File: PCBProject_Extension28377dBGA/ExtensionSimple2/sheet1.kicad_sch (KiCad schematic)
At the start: 86 parts, among them P1 Header 6X2, P2 Header 6X2, P3 Header 2X2, P4 Header 2X2, P5 Header 2X2, P6 Header 2X2, Q1 FMMT618TA, U1 SN74ABT541, U2 SN74ABT541

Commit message: block routing done.
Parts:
- removed P3, P4, P5, P6: Header 2X2, Connector_PinSocket_2.54mm:PinSocket_2x02_P2.54mm_Vertical, symbol sheet1-altium-import:root_0_Header 2X2
- added J1: Conn_02x08_Top_Bottom, Connector_PinSocket_2.54mm:PinSocket_2x08_P2.54mm_Vertical, symbol Connector_Generic:Conn_02x08_Odd_Even
- added J2 (x2): Conn_01x02_Pin, Connector_PinSocket_2.54mm:PinSocket_2x02_P2.54mm_Vertical, symbol Connector_Generic:Conn_02x02_Odd_Even
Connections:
- net AGND: now also J1.1 (Pin_1), J1.11 (Pin_11), J1.3 (Pin_3), J1.5 (Pin_5), J1.7 (Pin_7), J1.9 (Pin_9)
- net D12V1: now also J1.14 (Pin_14), J1.16 (Pin_16)
- net DC_BUS_2M1: now also J2.1 (Pin_1), J2.3 (Pin_3)
- net DC_BUS_2M2: now also J2.1 (Pin_1), J2.3 (Pin_3)
- net GND_2M1: now also J2.2 (Pin_2), J2.4 (Pin_4)
- net GND_2M2: now also J2.2 (Pin_2), J2.4 (Pin_4)
- net PWM1A_5V: now also J1.2 (Pin_2)
- net PWM1B_5V: now also J1.8 (Pin_8)
- net PWM2A_5V: now also J1.4 (Pin_4)
- net PWM2B_5V: now also J1.10 (Pin_10)
- net PWM3A_5V: now also J1.6 (Pin_6)
- net PWM3B_5V: now also J1.12 (Pin_12)
- new net D12VGND: J1.13 (Pin_13), J1.15 (Pin_15)
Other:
- note added: "PWM信号&供电"

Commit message: update sheet1
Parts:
- removed P1, P2: Header 6X2, Connector_PinSocket_2.54mm:PinSocket_2x06_P2.54mm_Vertical, symbol sheet1-altium-import:root_0_Header 6X2
- added INC2, SPI1: HIF3FC-20PA-2.54DSA, Connector_IDC:IDC-Header_2x10_P2.54mm_Vertical, symbol sheet1-altium-import:root_0_HIF3FC-20PA-2.54DSA
- added J1: Conn_02x08_Top_Bottom, Connector_PinSocket_2.54mm:PinSocket_2x08_P2.54mm_Vertical, symbol Connector_Generic:Conn_02x08_Odd_Even
- added RU3: 0R, mmlab-footprint-library:0805, symbol sheet1-altium-import:root_0_Res2
- added SPI2: Conn_02x04_Counter_Clockwise, Connector_PinSocket_2.54mm:PinSocket_2x04_P2.54mm_Vertical, symbol Connector_Generic:Conn_02x04_Counter_Clockwise
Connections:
- net A+5V: now also SPI1.18, SPI1.20
- net AGND: now also J1.1 (Pin_1), J1.11 (Pin_11), J1.3 (Pin_3), J1.5 (Pin_5), J1.7 (Pin_7), J1.9 (Pin_9), SPI1.5, SPI1.7, SPI2.5 (Pin_5), SPI2.6 (Pin_6)
- net D+5V: now also SPI1.14, SPI1.16, SPI2.3 (Pin_3), SPI2.4 (Pin_4)
- net D12V1: now also J1.14 (Pin_14), J1.16 (Pin_16)
- net D12VGND: now also J1.13 (Pin_13), J1.15 (Pin_15)
- net PE_GND: now also SPI1.6, SPI1.8
- net PWM4A_5V: now also J1.2 (Pin_2)
- net PWM4B_5V: now also J1.8 (Pin_8)
- net PWM5A_5V: now also J1.4 (Pin_4)
- net PWM5B_5V: now also J1.10 (Pin_10)
- net PWM6A_5V: now also J1.6 (Pin_6)
- net PWM6B_5V: now also J1.12 (Pin_12)
- net REF_3V: now also RU3.1
- net SPI B MI HS: now also SPI2.2 (Pin_2)
- net SPI B MO HS: now also SPI2.1 (Pin_1)
- net SPI_A_CK_HS: now also SPI1.11
- net SPI_A_MI_HS: now also SPI1.12
- net SPI_A_MO_HS: now also SPI1.9
- net SPI_B_CK_HS: now also SPI2.8 (Pin_8)
- net SPI_C_CK_HS: now also SPI1.3
- net SPI_C_MI_HS: now also SPI1.4
- net SPI_C_MO_HS: now also SPI1.1
- net ~{SPI_A_STE_HS}: now also SPI1.10
- net ~{SPI_B_STE_HS}: now also SPI2.7 (Pin_7)
- net ~{SPI_C_STE_HS}: now also SPI1.2
- new net: RU3.2, SPI1.13, SPI1.15
- new net -5V_ADC: SPI1.17, SPI1.19
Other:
- note added: "DAC"

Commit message: extension board layout
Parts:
- removed INC2: HIF3FC-20PA-2.54DSA, Connector_IDC:IDC-Header_2x10_P2.54mm_Vertical, symbol sheet1-altium-import:root_0_HIF3FC-20PA-2.54DSA
- added J1: Conn_02x05_Odd_Even, Connector_IDC:IDC-Header_2x05_P2.54mm_Vertical, symbol Connector_Generic:Conn_02x05_Odd_Even
- LEM1, LEM2: footprint Connector_IDC:IDC-Header_2x15_P2.54mm_Vertical -> Connector_PinSocket_2.54mm:PinSocket_2x15_P2.54mm_Vertical
- RU3: footprint mmlab-footprint-library:0805 -> Resistor_SMD:R_0805_2012Metric
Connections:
- net AGND: now also J1.9 (Pin_9)
- net D+5V: now also J1.10 (Pin_10)
- net MQEP1A: now also J1.2 (Pin_2)
- net MQEP1B: now also J1.4 (Pin_4)
- net MQEP1Z: now also J1.6 (Pin_6)
- net PE_GND: now also J1.7 (Pin_7)
- net QEP1_HALL_U: now also J1.1 (Pin_1)
- net QEP1_HALL_V: now also J1.3 (Pin_3)
- net QEP1_HALL_W: now also J1.5 (Pin_5)
- net VDD: now also J1.8 (Pin_8)
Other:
- moved on the sheet: J1

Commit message: HY加油
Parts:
- DSP1: footprint 1mmlab_footprint:DSP_240 -> 1mmlab_footprint:DSP_240_SMD
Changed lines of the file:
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@@
       (effects (font (size 1.27 1.27)))
     )
-    (property "Footprint" "1mmlab_footprint:DSP_240" (at 711.2 421.64 0)
+    (property "Footprint" "1mmlab_footprint:DSP_240_SMD" (at 711.2 421.64 0)
       (effects (font (size 1.27 1.27)) hide)
     )
@@
   )
   (symbol (lib_id "Connector_Generic:Conn_02x05_Odd_Even") (at 400.05 509.27 0) (unit 1)
-    (in_bom yes) (on_board yes) (dnp no) (fields_autoplaced)
+    (in_bom yes) (on_board yes) (dnp no)
     (property "Reference" "J1" (at 401.32 497.84 0)
       (effects (font (size 1.27 1.27)))
@@
       (effects (font (size 1.27 1.27)))
     )
-    (property "Footprint" "Connector_IDC:IDC-Header_2x05_P2.54mm_Vertical" (at 400.05 509.27 0)
-      (effects (font (size 1.27 1.27)) hide)
+    (property "Footprint" "Connector_IDC:IDC-Header_2x05_P2.54mm_Vertical" (at 400.05 518.16 0) (show_name)
+      (effects (font (size 1.27 1.27)))
     )
     (property "Datasheet" "~" (at 400.05 509.27 0)

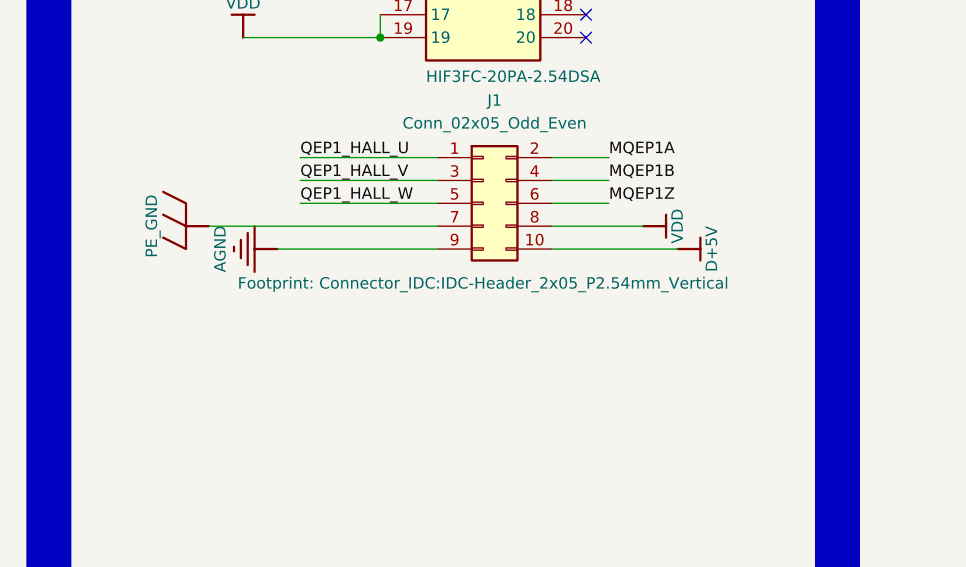
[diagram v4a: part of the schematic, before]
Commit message: Revert "HY加油"
This reverts commit aaa1912d429fb000e99d7c8797d7335188b5b639.

rollback
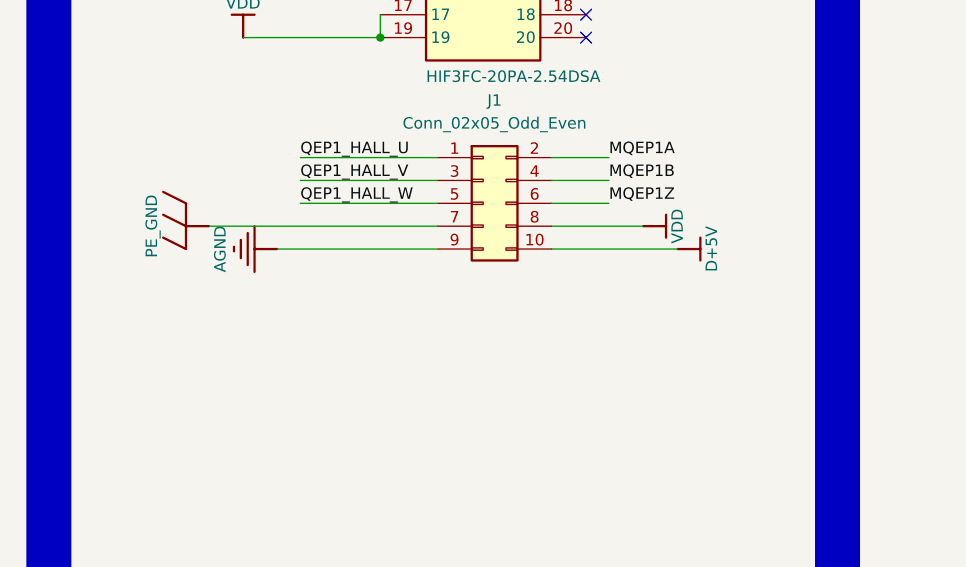
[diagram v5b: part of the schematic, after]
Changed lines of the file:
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@@
   )
   (symbol (lib_id "Connector_Generic:Conn_02x05_Odd_Even") (at 400.05 509.27 0) (unit 1)
-    (in_bom yes) (on_board yes) (dnp no)
+    (in_bom yes) (on_board yes) (dnp no) (fields_autoplaced)
     (property "Reference" "J1" (at 401.32 497.84 0)
       (effects (font (size 1.27 1.27)))
@@
       (effects (font (size 1.27 1.27)))
     )
-    (property "Footprint" "Connector_IDC:IDC-Header_2x05_P2.54mm_Vertical" (at 400.05 518.16 0) (show_name)
-      (effects (font (size 1.27 1.27)))
+    (property "Footprint" "Connector_IDC:IDC-Header_2x05_P2.54mm_Vertical" (at 400.05 509.27 0)
+      (effects (font (size 1.27 1.27)) hide)
     )
     (property "Datasheet" "~" (at 400.05 509.27 0)

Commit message: submit extension board
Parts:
- R21, R22: value 1k -> 1K
- R31: value 301R -> 1K
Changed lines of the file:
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@@
       (effects (font (size 1.27 1.27)) (justify left bottom))
     )
-    (property "Value" "1k" (at 420.37 135.001 0)
+    (property "Value" "1K" (at 420.37 135.001 0)
       (effects (font (size 1.27 1.27)) (justify left bottom))
     )
@@
     )
     (property "ALTIUM_VALUE" "1K" (at 420.37 137.541 0)
-      (effects (font (size 1.27 1.27)) (justify left bottom))
+      (effects (font (size 1.27 1.27)) (justify left bottom) hide)
     )
     (pin "1")
@@
       (effects (font (size 1.27 1.27)) (justify left bottom))
     )
-    (property "Value" "10K" (at 659.257 86.614 0)
+    (property "Value" "10K" (at 661.67 91.44 0)
       (effects (font (size 1.27 1.27)) (justify left bottom))
     )
@@
       (effects (font (size 1.27 1.27)) (justify left bottom))
     )
-    (property "Value" "301R" (at 676.529 69.342 0)
+    (property "Value" "1K" (at 679.45 77.47 0)
       (effects (font (size 1.27 1.27)) (justify left bottom))
     )
@@
       (effects (font (size 1.27 1.27)) (justify left bottom))
     )
-    (property "Value" "1k" (at 420.37 71.501 0)
+    (property "Value" "1K" (at 420.37 71.501 0)
       (effects (font (size 1.27 1.27)) (justify left bottom))
     )
@@
     )
     (property "ALTIUM_VALUE" "1K" (at 420.37 74.041 0)
-      (effects (font (size 1.27 1.27)) (justify left bottom))
+      (effects (font (size 1.27 1.27)) (justify left bottom) hide)
     )
     (pin "1")
